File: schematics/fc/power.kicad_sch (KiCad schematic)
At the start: 36 parts, among them Q10 DMN1150UFB-7B, U10 NCV8187AMT180TAG, U11 LP5912-3.3DRVR, U7 LMR51420YFDDCR, U8 LMR51420YFDDCR, U9 TPS2116DRLR

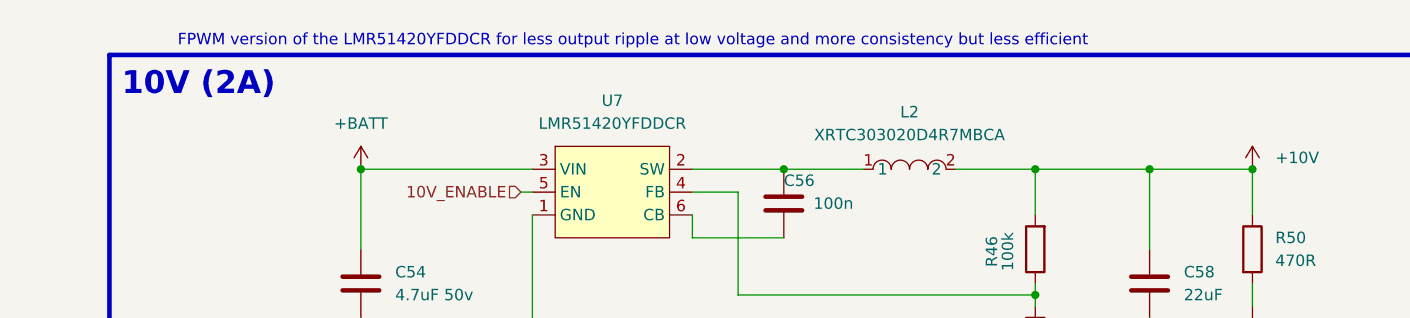
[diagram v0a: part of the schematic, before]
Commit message: checkpoint: Bluejay/BLHeli_S part imports + ESC rework notes
EFM8BB51F16G (C6547511), AGM310MAP (C5184858), BY25Q64ESCIG (C50176394)
imported into libs/lib.kicad_sym + lib.pretty + lib.3dshapes.
BLHELI_S_ESC_NOTES.md documents gate-drive research (1S direct drive vs
2S level-shift requirement) and open design decisions.

Co-Authored-By: Claude Fable 5 <noreply@anthropic.com>
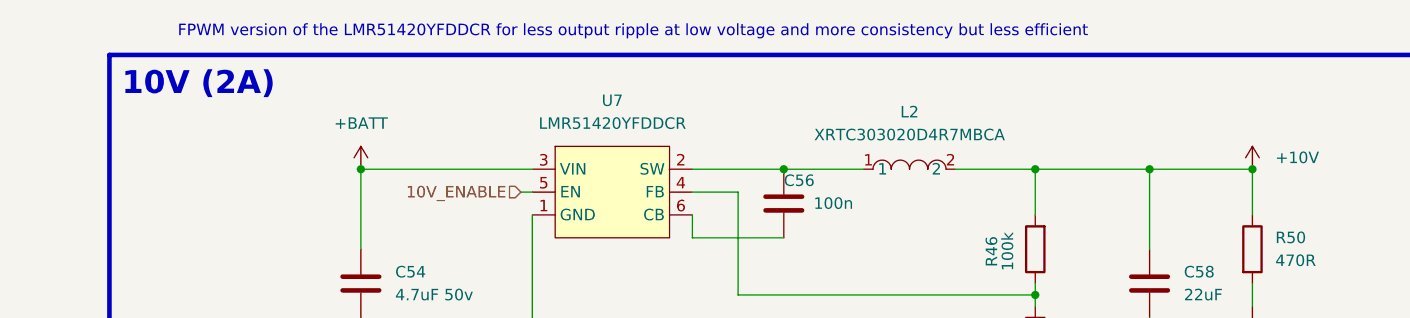
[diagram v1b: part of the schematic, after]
